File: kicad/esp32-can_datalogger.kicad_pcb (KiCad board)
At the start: 2 copper layers, 60 x 40 mm, 22 parts, among them J1 USB_C_Receptacle_USB2.0_16P, J2 USB_C_Receptacle_USB2.0_16P, J3 USB_C_Receptacle_USB2.0_16P, J4 USB_C_Receptacle_USB2.0_16P, J5 MSD-4-A, U5 TJA1051T, U6 TJA1051T

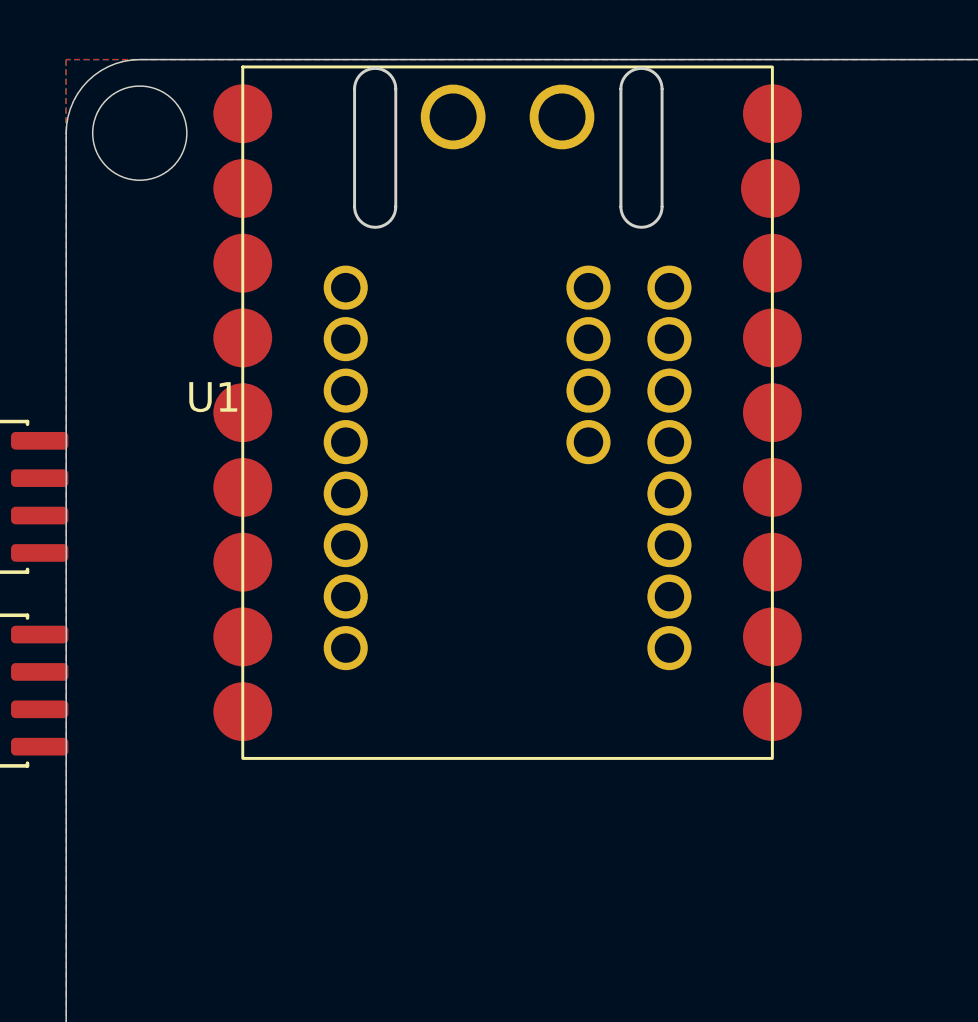
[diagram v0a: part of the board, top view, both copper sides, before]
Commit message: switch to esp32-c6
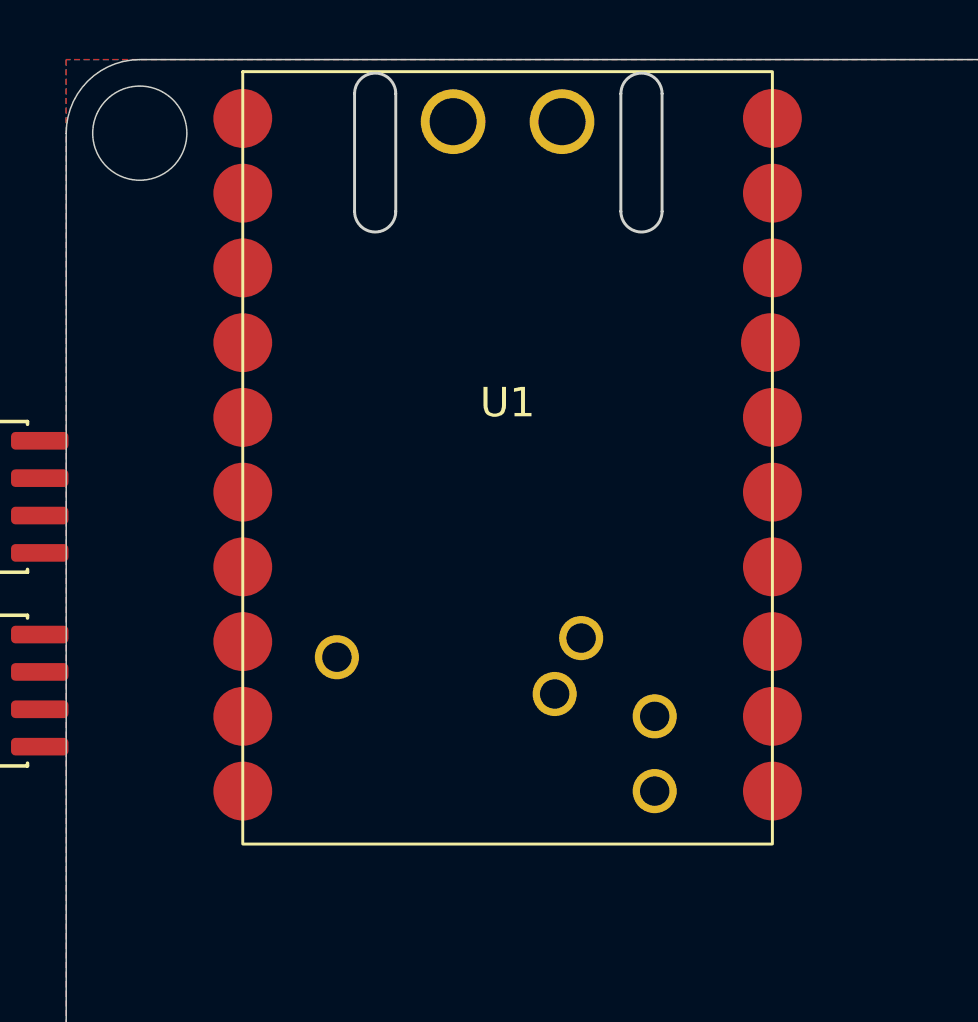
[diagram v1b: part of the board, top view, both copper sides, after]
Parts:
- U1: footprint esp32-can_datalogger:ESP32-S3 Supermini -> esp32-can_datalogger:ESP32-C6 Supermini
- moved U1 0.16 mm to (85.0, 92.2)
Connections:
- U1 pad 12: /C1SX -> unconnected-(U1-GPIO9-Pad12)
- U1 pad 13: /C1RX -> unconnected-(U1-GPIO14-Pad13)
- U1 pad 14: /C1TX -> unconnected-(U1-GPIO15-Pad14)
- U1 pad 16: +3.3V -> unconnected-(U1-GPIO19-Pad16)
- U1 pad 17: GND -> unconnected-(U1-GPIO20-Pad17)
- U1 pad 18: +5V -> unconnected-(U1-3V3-Pad18)
- U1 pad 19: +5V -> unconnected-(U1-GND-Pad19)
- U1 pad 20: GND -> unconnected-(U1-5V-Pad20)
- U1 pad 21: /C2TX -> unconnected-(U1-B+-Pad21)
- U1 pad 22: /C2RX -> unconnected-(U1-B--Pad22)
- U1 pad 23: /C2SX -> unconnected-(U1-GPIO12-Pad23)

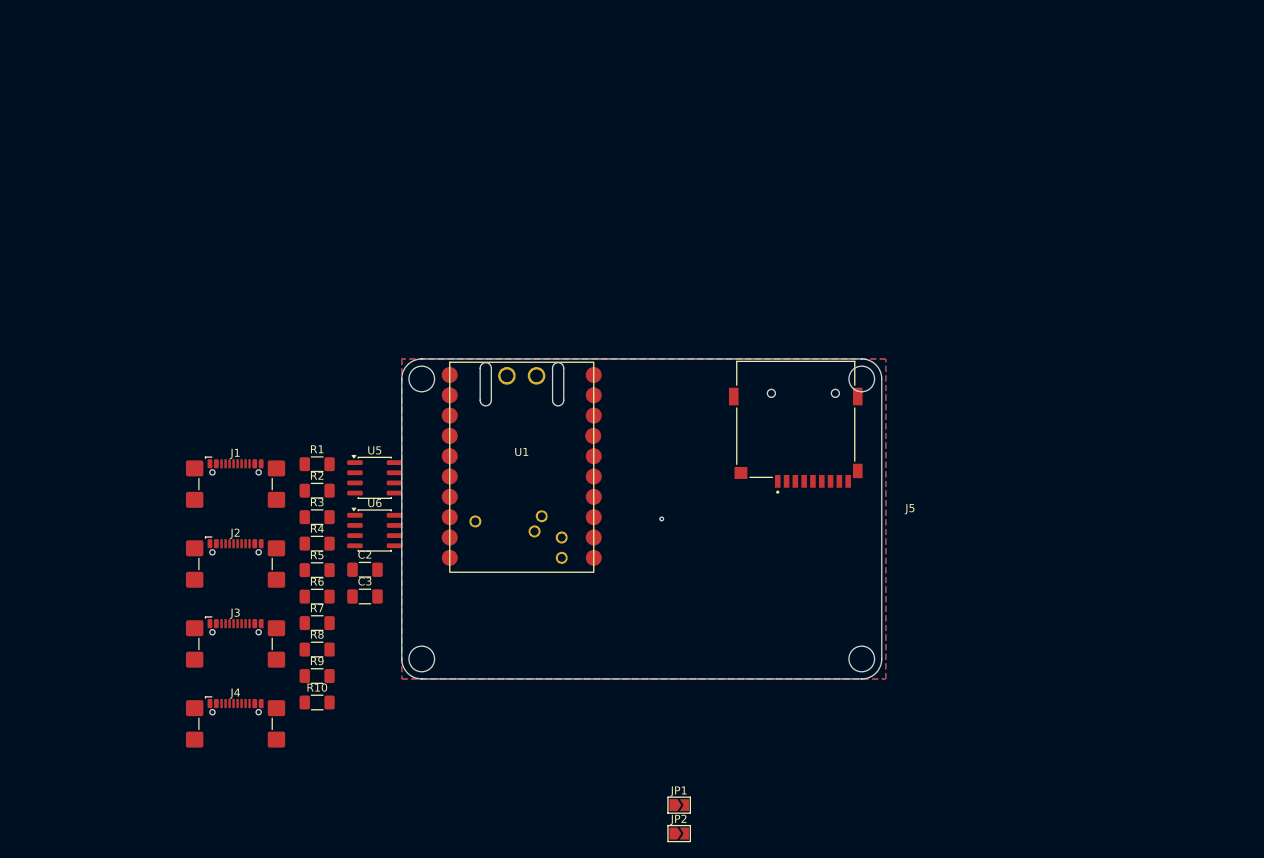
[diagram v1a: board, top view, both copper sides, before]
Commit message: add footprints, change to bidir TTL, make connections on c6
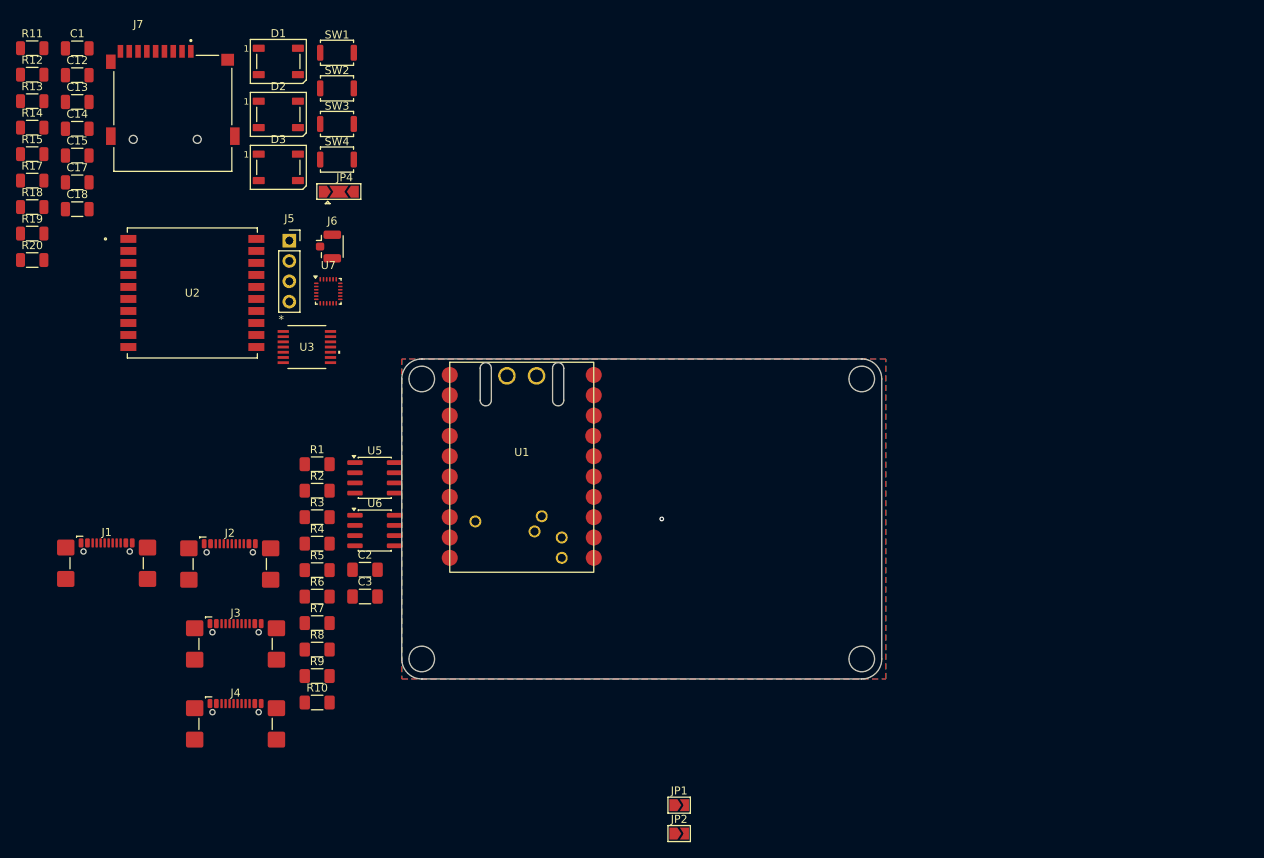
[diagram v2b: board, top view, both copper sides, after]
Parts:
- added C1: 1uF, Capacitor_SMD:C_1206_3216Metric, F.Cu at (29.4, 41.2)
- added C12: 0.1uF, Capacitor_SMD:C_1206_3216Metric, F.Cu at (29.4, 44.5)
- added C13: 0.1uF, Capacitor_SMD:C_1206_3216Metric, F.Cu at (29.4, 47.9)
- added C14: 0.1uF, Capacitor_SMD:C_1206_3216Metric, F.Cu at (29.4, 51.2)
- added C15: 0.1uF, Capacitor_SMD:C_1206_3216Metric, F.Cu at (29.4, 54.6)
- added C17: 0.1uF, Capacitor_SMD:C_1206_3216Metric, F.Cu at (29.4, 57.9)
- added C18: 0.1uF, Capacitor_SMD:C_1206_3216Metric, F.Cu at (29.4, 61.3)
- added D1: WS2812B, LED_SMD:LED_WS2812B_PLCC4_5.0x5.0mm_P3.2mm, F.Cu at (54.6, 42.8)
- added D2: WS2812B, LED_SMD:LED_WS2812B_PLCC4_5.0x5.0mm_P3.2mm, F.Cu at (54.6, 49.4)
- added D3: WS2812B, LED_SMD:LED_WS2812B_PLCC4_5.0x5.0mm_P3.2mm, F.Cu at (54.6, 56.0)
- added J6: Conn_Coaxial, Connector_Coaxial:U.FL_Hirose_U.FL-R-SMT-1_Vertical, F.Cu at (61.3, 65.9)
- added J7: MicroSD, esp32-can_datalogger:CUI_MSD-4-A, F.Cu at (41.4, 49.3)
- added JP4: SolderJumper_3_Open, Jumper:SolderJumper-3_P2.0mm_Open_TrianglePad1.0x1.5mm, F.Cu at (62.1, 59.1)
- added R11: 470, Resistor_SMD:R_1206_3216Metric, F.Cu at (23.8, 41.2)
- added R12: 470, Resistor_SMD:R_1206_3216Metric, F.Cu at (23.8, 44.5)
- added R13: 470, Resistor_SMD:R_1206_3216Metric, F.Cu at (23.8, 47.8)
- added R14: 10K, Resistor_SMD:R_1206_3216Metric, F.Cu at (23.8, 51.1)
- added R15: 10K, Resistor_SMD:R_1206_3216Metric, F.Cu at (23.8, 54.4)
- added R17: 47k, Resistor_SMD:R_1206_3216Metric, F.Cu at (23.8, 57.7)
- added R18: 16k, Resistor_SMD:R_1206_3216Metric, F.Cu at (23.8, 61.0)
- added R19: 30k, Resistor_SMD:R_1206_3216Metric, F.Cu at (23.8, 64.3)
- added R20: 91k, Resistor_SMD:R_1206_3216Metric, F.Cu at (23.8, 67.6)
- added SW1: SW_Push, Button_Switch_SMD:SW_Push_SPST_NO_Alps_SKRK, F.Cu at (61.9, 41.7)
- added SW2: SW_Push, Button_Switch_SMD:SW_Push_SPST_NO_Alps_SKRK, F.Cu at (61.9, 46.2)
- added SW3: SW_Push, Button_Switch_SMD:SW_Push_SPST_NO_Alps_SKRK, F.Cu at (61.9, 50.6)
- added SW4: SW_Push, Button_Switch_SMD:SW_Push_SPST_NO_Alps_SKRK, F.Cu at (61.9, 55.1)
- added U2: PA1616D, esp32-can_datalogger:CD-PA1616D_ADA, F.Cu at (43.8, 71.8)
- added U3: PI4ULS3V204LEX, esp32-can_datalogger:SOIC_3V204LEX_DIO, F.Cu at (58.1, 78.5)
- added U7: ICM-20948, Sensor_Motion:InvenSense_QFN-24_3x3mm_P0.4mm, F.Cu at (60.8, 71.5)
- J5: value MSD-4-A -> Conn_01x04_Socket; footprint esp32-can_datalogger:CUI_MSD-4-A -> Connector_PinSocket_2.54mm:PinSocket_1x04_P2.54mm_Vertical
- moved J5 67.1 mm to (55.9, 65.2), turned to 0 degrees
- moved J1 18.9 mm to (33.1, 106.7)
- moved J2 0.73 mm to (48.5, 106.8)
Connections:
- J1 pad A6: /CAN1H -> /CAN0H
- J1 pad A7: /CAN1L -> /CAN0L
- J1 pad B6: /CAN1H -> /CAN0H
- J1 pad B7: /CAN1L -> /CAN0L
- J2 pad A6: /CAN2H -> /CAN0H
- J2 pad A7: /CAN2L -> /CAN0L
- J2 pad B6: /CAN2H -> /CAN0H
- J2 pad B7: /CAN2L -> /CAN0L
- J3 pad A6: /CAN2H -> /CAN1H
- J3 pad A7: /CAN2L -> /CAN1L
- J3 pad B6: /CAN2H -> /CAN1H
- J3 pad B7: /CAN2L -> /CAN1L
- J4 pad A6: /CAN1H -> /CAN0H
- J4 pad A7: /CAN1L -> /CAN0L
- J4 pad B6: /CAN1H -> /CAN0H
- J4 pad B7: /CAN1L -> /CAN0L
- J5 pad 1: unconnected-(J5-DAT2-Pad1) -> I2C_SDA
- J5 pad 2: unconnected-(J5-CD/DAT3-Pad2) -> I2C_SCK
- J5 pad 3: unconnected-(J5-CMD-Pad3) -> +3.3V
- J5 pad 4: unconnected-(J5-VDD-Pad4) -> GND
- JP1 pad 1: /CAN1L -> /CAN0L
- JP2 pad 1: /CAN2L -> /CAN1L
- R3 pad 2: /CAN1H -> /CAN0H
- R6 pad 2: /CAN2H -> /CAN1H
- U1 pad 1: unconnected-(U1-TX-Pad1) -> GPS_TX
- U1 pad 10: unconnected-(U1-GPIO7-Pad10) -> SCK
- U1 pad 12: unconnected-(U1-GPIO9-Pad12) -> ARGB_DIN
- U1 pad 13: unconnected-(U1-GPIO14-Pad13) -> GPS_FIX
- U1 pad 14: unconnected-(U1-GPIO15-Pad14) -> Net-(JP4-B)
- U1 pad 15: unconnected-(U1-GPIO18-Pad15) -> CS_SD
- U1 pad 16: unconnected-(U1-GPIO19-Pad16) -> I2C_SCK
- U1 pad 17: unconnected-(U1-GPIO20-Pad17) -> I2C_SDA
- U1 pad 18: unconnected-(U1-3V3-Pad18) -> +3.3V
- U1 pad 19: unconnected-(U1-GND-Pad19) -> GND
- U1 pad 2: unconnected-(U1-RX-Pad2) -> GPS_RX
- U1 pad 20: unconnected-(U1-5V-Pad20) -> +5V
- U1 pad 21: unconnected-(U1-B+-Pad21) -> +5V
- U1 pad 22: unconnected-(U1-B--Pad22) -> GND
- U1 pad 25: unconnected-(U1-GPIO21-Pad25) -> SD_CD
- U1 pad 26: unconnected-(U1-GPIO22-Pad26) -> BUTS
- U1 pad 3: unconnected-(U1-GPIO0-Pad3) -> /C0TX
- U1 pad 4: unconnected-(U1-GPIO1-Pad4) -> /C0RX
- U1 pad 5: unconnected-(U1-GPIO2-Pad5) -> /C1TX
- U1 pad 6: unconnected-(U1-GPIO3-Pad6) -> /C1RX
- U1 pad 7: unconnected-(U1-GPIO4-Pad7) -> CS_IMU
- U1 pad 8: unconnected-(U1-GPIO5-Pad8) -> MOSI
- U1 pad 9: unconnected-(U1-GPIO6-Pad9) -> MISO
- U5 pad 1: /C1TX -> /C0TX
- U5 pad 4: /C1RX -> /C0RX
- U5 pad 6: /CAN1L -> /CAN0L
- U5 pad 7: /CAN1H -> /CAN0H
- U5 pad 8: /C1SX -> /C0SX
- U6 pad 1: /C2TX -> /C1TX
- U6 pad 4: /C2RX -> /C1RX
- U6 pad 6: /CAN2L -> /CAN1L
- U6 pad 7: /CAN2H -> /CAN1H
- U6 pad 8: /C2SX -> /C0SX

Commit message: pcb updates
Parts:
- added J8: USB_C_Receptacle_USB2.0_16P, Connector_USB:USB_C_Receptacle_GCT_USB4110, F.Cu at (121.4, 126.5)
- added J9: USB_C_Receptacle_USB2.0_16P, Connector_USB:USB_C_Receptacle_GCT_USB4110, F.Cu at (136.4, 126.5)
- added R16: 5K1, Resistor_SMD:R_1206_3216Metric_Pad1.30x1.75mm_HandSolder, F.Cu at (116.8, 119.5)
- added R21: 5K1, Resistor_SMD:R_1206_3216Metric_Pad1.30x1.75mm_HandSolder, F.Cu at (125.8, 119.5)
- added R22: 5K1, Resistor_SMD:R_1206_3216Metric_Pad1.30x1.75mm_HandSolder, F.Cu at (131.8, 119.5)
- added R23: 5K1, Resistor_SMD:R_1206_3216Metric_Pad1.30x1.75mm_HandSolder, F.Cu at (140.8, 119.5)
- J7: moved to B.Cu
- moved R20 124.4 mm to (140.0, 112.0), turned to -90 degrees
- moved R19 111.9 mm to (125.0, 112.0), turned to -90 degrees
- moved R17 110.5 mm to (125.0, 102.0), turned to -90 degrees
- moved SW4 101.0 mm to (145.0, 112.5)
- moved R18 100.2 mm to (110.0, 112.0), turned to -90 degrees
- moved SW3 92.0 mm to (130.0, 112.5)
- moved SW1 91.3 mm to (130.0, 102.5)
- moved SW2 85.0 mm to (115.0, 112.5)
- moved J7 75.2 mm to (111.3, 76.8)
- moved D1 61.9 mm to (107.5, 75.0), turned to -90 degrees
- moved J3 58.0 mm to (106.4, 126.5)
- moved JP4 55.3 mm to (91.5, 106.0), turned to 180 degrees
- moved U3 55.2 mm to (109.0, 100.0)
- moved D2 52.1 mm to (100.0, 75.0), turned to -90 degrees
- moved R8 51.5 mm to (110.8, 119.5)
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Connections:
- J3 pad A6: /CAN1H -> /CAN0H
- J3 pad A7: /CAN1L -> /CAN0L
- J3 pad B6: /CAN1H -> /CAN0H
- J3 pad B7: /CAN1L -> /CAN0L
- J4 pad A6: /CAN0H -> /CAN1H
- J4 pad A7: /CAN0L -> /CAN1L
- J4 pad B6: /CAN0H -> /CAN1H
- J4 pad B7: /CAN0L -> /CAN1L
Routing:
- net Net-(D2-DOUT): track 0.00 -> 6.86 mm
- net Net-(D1-DOUT): track 0.00 -> 6.64 mm
- net Net-(JP2-B): track 0.00 -> 3.45 mm
- net Net-(JP1-B): track 0.00 -> 3.45 mm
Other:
- board size 60 x 40 mm -> 100 x 60 mm

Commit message: pcb update
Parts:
- R1, R10, R16, R2, R21, R22, R23, R4, R5, R7, R8, R9: moved to B.Cu
- moved C15 115.7 mm to (135.0, 102.0), turned to 90 degrees
- moved C14 89.8 mm to (101.0, 105.5), turned to 90 degrees
- moved C13 88.6 mm to (104.5, 95.0)
- moved C12 87.3 mm to (104.5, 89.0), turned to 180 degrees
- moved C17 87.0 mm to (105.0, 101.0), turned to 180 degrees
- moved C18 82.0 mm to (98.5, 105.5), turned to 90 degrees
- moved C1 65.1 mm to (73.0, 89.5)
- moved R11 62.1 mm to (73.5, 78.4)
- moved R12 62.1 mm to (73.5, 81.7)
- moved R13 62.1 mm to (73.5, 85.0)
- moved R14 59.4 mm to (63.5, 95.2)
- moved R15 59.4 mm to (63.5, 98.5)
- moved J6 23.6 mm to (62.0, 73.5), turned to 90 degrees
- moved U5 17.0 mm to (82.0, 112.5), turned to 180 degrees
- moved U6 16.0 mm to (68.0, 112.5), turned to 180 degrees
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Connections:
- C1 pad 2: +3V3 -> +3.3V
- U2 pad 1: +3V3 -> +3.3V
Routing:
- net +5V: track 0.00 -> 166.8 mm, vias 0 -> 12
- net /CAN0H: track 0.00 -> 109.8 mm
- net /CAN0L: track 0.00 -> 108.0 mm
- net BUTS: track 0.00 -> 39.1 mm
- net /C0SX: track 0.00 -> 38.3 mm
- net GND: track 0.00 -> 19.1 mm
- net Net-(R19-Pad2): track 0.00 -> 16.2 mm
- net Net-(R18-Pad2): track 0.00 -> 16.2 mm
- net /CAN1H: track 0.00 -> 15.3 mm
- net /CAN1L: track 0.00 -> 13.4 mm
- net /MISO_1V8: track 0.00 -> 11.8 mm
- net +3V3: track 0.00 -> 11.6 mm
- net +1V8: track 0.00 -> 4.95 mm, vias 0 -> 2
- net Net-(J8-CC1): track 0.00 -> 4.05 mm, vias 0 -> 1
- net Net-(J3-CC1): track 0.00 -> 4.04 mm, vias 0 -> 1
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
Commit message: more
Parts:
- moved R14 50.7 mm to (112.5, 82.0), turned to 90 degrees
- moved R15 44.2 mm to (104.5, 82.0), turned to 90 degrees
- moved R11 7.18 mm to (74.5, 85.5)
- moved R13 4.59 mm to (74.5, 80.5)
- moved R12 4.29 mm to (74.5, 77.5)
- moved C1 2.49 mm to (74.5, 91.5), turned to 180 degrees
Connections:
- C12 pad 2: +3V3 -> +3.3V
- C17 pad 2: +3V3 -> +3.3V
- D1 pad 1: VOUT -> +3.3V
- D2 pad 1: VOUT -> +3.3V
- D3 pad 1: VOUT -> +3.3V
- J7 pad 4: +3V3 -> +3.3V
- R14 pad 2: +3V3 -> +3.3V
- R15 pad 2: +3V3 -> +3.3V
- U3 pad 1: +3V3 -> +3.3V
- U3 pad 8: +3V3 -> +3.3V
- U7 pad 13: +3V3 -> +3.3V
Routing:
- net +3.3V: track 0.00 -> 145.8 mm, vias 0 -> 5
- net GPS_FIX: track 0.00 -> 78.0 mm, vias 0 -> 2
- net GPS_TX: track 0.00 -> 57.5 mm
- net GPS_RX: track 0.00 -> 52.3 mm
- net SCK: track 0.00 -> 34.1 mm, vias 0 -> 2
- net CS_SD: track 0.00 -> 32.9 mm, vias 0 -> 3
- net CS_IMU: track 0.00 -> 27.1 mm
- net +3V3: track 11.6 -> 0.00 mm
- net MISO: track 0.00 -> 11.5 mm, vias 0 -> 2
- net Net-(J6-In): track 0.00 -> 10.2 mm
- net Net-(U2-TX0): track 0.00 -> 4.42 mm
- net Net-(U2-RX0): track 0.00 -> 4.20 mm
- net Net-(U2-3D-FIX): track 0.00 -> 4.05 mm
- net SD_CD: track 0.00 -> 1.16 mm, vias 0 -> 1
- net MOSI: vias 0 -> 1
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
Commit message: add vreg
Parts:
- added C4: 10uF, Capacitor_SMD:C_1206_3216Metric, F.Cu at (172.3, 94.9)
- added C5: 22uF, Capacitor_SMD:C_1206_3216Metric, F.Cu at (172.3, 98.3)
- added U4: AZ1117-1.8, Package_TO_SOT_SMD:SOT-223-3_TabPin2, F.Cu at (171.7, 85.7)

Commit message: update
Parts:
- R15: moved to B.Cu
- moved C4 88.3 mm to (84.7, 105.0)
- moved U4 86.0 mm to (86.8, 99.7)
- moved C5 79.2 mm to (93.2, 98.0), turned to 90 degrees
- moved R14 34.3 mm to (146.8, 83.0)
- moved R15 3.73 mm to (101.0, 83.3)
- moved D1 2.55 mm to (107.5, 77.5)
- moved D2 2.55 mm to (100.0, 77.5)
- moved D3 2.55 mm to (92.5, 77.5)
- moved JP4 1.50 mm to (92.5, 108.0)
- moved C2 1.12 mm to (88.5, 112.0), turned to 180 degrees
- moved C3 1.12 mm to (74.5, 112.0), turned to 180 degrees
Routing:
- net /C0RX: track 0.00 -> 75.7 mm
- net /C1TX: track 0.00 -> 72.2 mm, vias 0 -> 2
- net /C0TX: track 0.00 -> 69.8 mm
- net /C1RX: track 0.00 -> 67.3 mm, vias 0 -> 2
- net I2C_SCK: track 0.00 -> 64.1 mm, vias 0 -> 3
- net I2C_SDA: track 0.00 -> 62.8 mm, vias 0 -> 3
- net Net-(JP4-B): track 0.00 -> 59.4 mm, vias 0 -> 2
- net ARGB_DIN: track 0.00 -> 47.3 mm, vias 0 -> 2
- net SD_CD: track 1.16 -> 44.7 mm, vias 1 -> 2
- net +5V: track 166.8 -> 209.1 mm, vias 12 -> 15
- net +3.3V: track 145.8 -> 187.8 mm, vias 5 -> 6
- net MOSI: track 0.00 -> 33.2 mm
- net MISO: track 11.5 -> 34.0 mm
- net +1V8: track 4.95 -> 21.7 mm, vias 2 -> 3
- net GPS_RX: track 52.3 -> 53.8 mm
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
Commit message: remove DRC errors and warnings
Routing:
- net GND: track 19.1 -> 59.1 mm, vias 5 -> 27
- net +3.3V: track 187.8 -> 210.4 mm
- net +1V8: track 21.7 -> 32.7 mm
- net GPS_FIX: track 78.0 -> 86.2 mm, vias 2 -> 4
- net Net-(J9-CC1): track 0.00 -> 4.26 mm, vias 0 -> 1
- net Net-(J9-CC2): track 0.00 -> 3.80 mm, vias 0 -> 1
- net CS_IMU: track 28.4 -> 27.9 mm
- net /MISO_1V8: track 11.8 -> 11.5 mm, vias 0 -> 2
- net (no net): vias 0 -> 1
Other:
- board text added: "CAN0 ->"
- board text added: "CAN1"
- board text added: "Tanmay Chhatbar ESP32-C6 CAN Datalogger"
